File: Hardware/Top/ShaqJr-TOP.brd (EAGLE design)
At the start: 38 x 38 mm, 65 parts, among them SW3 SWITCH.MOM, SW4 SWITCH.MOM, U1 NRF52832_MODULE_MDBT42, U2 PCF8523, U3 FT231XS, Y1 32.768kHz, Y2 32.7680kHz

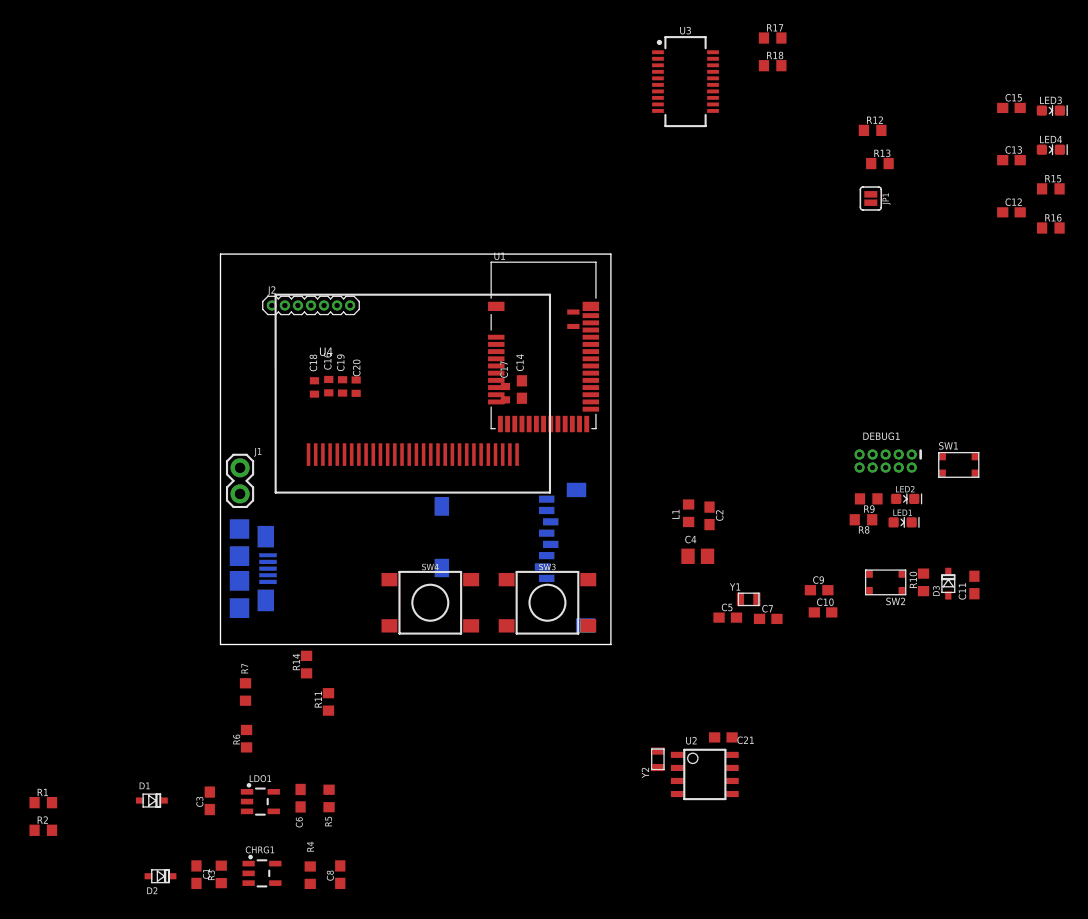
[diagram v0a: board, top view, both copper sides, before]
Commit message: completed take 007, may need to review polygons- gnd and 3.3v
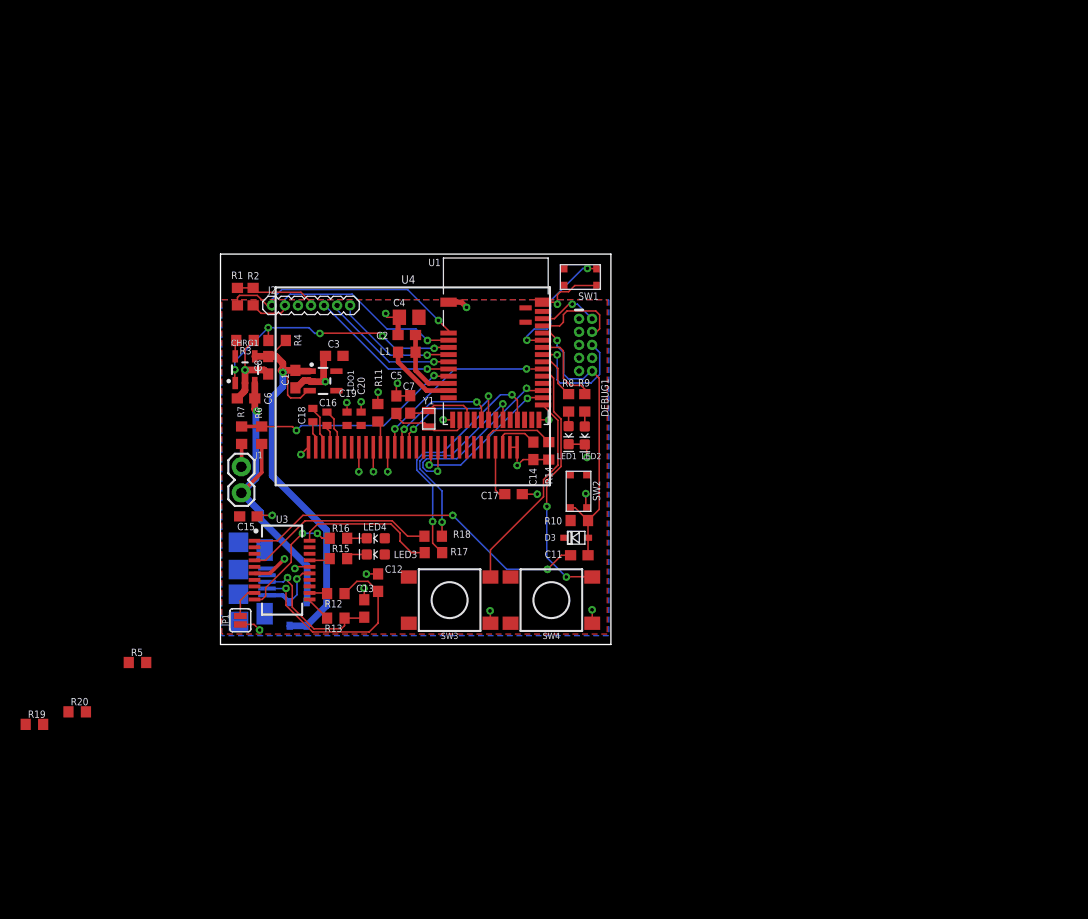
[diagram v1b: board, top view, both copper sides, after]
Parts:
- removed C10, C9: 300p, LinnesLab-Passives:C0603
- removed C21: 1u, LinnesLab-Passives:C0603
- removed SD1: (no value), LinnesLab-Connectors:MICROSD
- removed U2: PCF8523, LinnesLab-Clocks:SO8
- removed Y2: 32.7680kHz, LinnesLab-Clocks:2-SMD.NOLEAD.2.0MMTO1.2MM
- added R19, R20: 100k, LinnesLab-Passives:R0603
- C1: value 4.7u -> 1u
- C17: device LinnesLab-Passives:C0402 -> LinnesLab-Passives:C0603
- C6: value 1u -> 4.7u
- R3: value 100k -> (none)
- R4: value (none) -> 100k
- moved C15 84.2 mm to (2.72, 12.5), turned to 180 degrees
- moved LED3 78.6 mm to (15.1, 8.76), turned to 180 degrees
- moved R15 78.1 mm to (11.5, 8.36)
- moved C13 76.6 mm to (14.0, 3.51), turned to 90 degrees
- moved LED4 75.8 mm to (15.1, 10.3), turned to 180 degrees
- moved R16 75.6 mm to (11.5, 10.3)
- moved JP1 73.8 mm to (1.93, 2.36), turned to 90 degrees
- moved C12 71.4 mm to (15.3, 6.02), turned to 270 degrees
- moved R12 69.0 mm to (11.2, 4.95), turned to 180 degrees
- moved R13 69.0 mm to (11.2, 2.57), turned to 180 degrees
- moved U3 61.7 mm to (5.99, 7.24)
- moved R17 60.0 mm to (20.7, 8.94)
- moved R18 56.5 mm to (20.7, 10.5)
- moved R2 55.8 mm to (3.17, 33.9), turned to 90 degrees
- moved R1 52.8 mm to (1.65, 33.9), turned to 90 degrees
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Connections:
- removed net A6/TIA: J2.6, U1.7
- removed net A7/PPG: J2.7, U1.8
- removed net CD2: SD1.CD2
- removed net D29/LED.CTRL: J2.5, U1.6
- removed net N$2: R18.1
- removed net N$22: U2.1, Y2.P$2
- removed net N$3: R2.1
- removed net N$5: U2.2, Y2.P$1
- removed net VBAT: U2.3
- new net A4/PPG: J2.7, U1.5
- new net A5/TIA: J2.6, U1.6
- new net A7/BATT: R6.1, R7.2, U1.8
- new net D30/LED.CTRL: J2.5, U1.7
- net 3.3V: now also C3.1, R20.2; no longer C21.1, C6.1, R5.2, SD1.4, U2.8
- net A4/BATT: now also R19.2, R5.1; no longer R6.1, R7.2, U1.5
- net D27/CHRG.STATUS: now also R4.1; no longer R3.1
- net D5/CD1: no longer SD1.CD1
- net D7/SD.CS: no longer SD1.2
- net GND: now also C3.2, C8.1, R19.1, R20.1, R3.1; no longer C10.2, C21.2, C3.1, C8.2, C9.2, R4.1, R5.1, SD1.6, SD1.MT1, SD1.MT2, U2.4
- net MISO: no longer SD1.7
- net MOSI: no longer SD1.3
- net N$17: now also R3.2; no longer R4.2
- net P0.09/NFC1: no longer C9.1
- net P0.10/NFC2: no longer C10.1
- net RXD.FT: now also R18.1
- net SCK: no longer SD1.5
- net SCL: now also R2.1; no longer U2.6
- net SDA: no longer U2.5
- net VIN: now also C8.2, R4.2; no longer C3.2, R3.2
- net VLIPO: now also C6.1, R5.2; no longer C8.1
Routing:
- net GND: track 0.00 -> 67.2 mm, vias 0 -> 25
- net VIN: track 0.00 -> 44.1 mm, vias 0 -> 1
- net DTR: track 0.00 -> 34.5 mm, vias 0 -> 2
- net VLIPO: track 0.00 -> 30.3 mm, vias 0 -> 1
- net RESET: track 0.00 -> 29.5 mm, vias 0 -> 1
- net D27/CHRG.STATUS: track 0.00 -> 26.4 mm, vias 0 -> 5
- net SDA: track 0.00 -> 24.7 mm, vias 0 -> 1
- net D15/SW2: track 0.00 -> 24.7 mm, vias 0 -> 2
- net RXD.NRF: track 0.00 -> 24.6 mm, vias 0 -> 2
- net SCL: track 0.00 -> 22.5 mm, vias 0 -> 1
- net A7/BATT: track 0.00 -> 22.5 mm, vias 0 -> 2
- net USB-: track 0.00 -> 21.2 mm, vias 0 -> 1
- net TXD.NRF: track 0.00 -> 20.2 mm, vias 0 -> 2
- net D11/SW1: track 0.00 -> 20.1 mm
- net MOSI: track 0.00 -> 19.2 mm, vias 0 -> 2
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- added copper zone on layer 1, net 3.3V
- added copper zone on layer 16, net GND

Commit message: Finished Take 008
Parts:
- removed C19, C20: 2.2uF, LinnesLab-Passives:C0402
- removed R18: 0, LinnesLab-Passives:R0603
- removed R19, R20: 100k, LinnesLab-Passives:R0603
- removed U4: (no value), LinnesLab-Displays:UG-2864HSWEG01_0.96IN_NO-WRAPAROUND
- added C10: 47p, LinnesLab-Passives:C0603
- added C9: 100n, LinnesLab-Passives:C0603
- added U2: FT231XS, LinnesLab-DigitalIC:SSOP20_L
- C1: value 1u -> 4.7u
- C11: value 100n -> 47p
- C12: value 47p -> 10uF
- C13: value 47p -> 100n
- C14: value 10uF -> 2.2uF; device LinnesLab-Passives:C0603 -> LinnesLab-Passives:C0402
- C15: value 100n -> 2.2uF
- C17: device LinnesLab-Passives:C0603 -> LinnesLab-Passives:C0402
- C6: value 4.7u -> 1u
- R11: value 10k -> 27
- R13: value 27 -> 390k
- R14: value 390k -> 1k
- R16: value 1k -> 0
- R3: value (none) -> 100k
- R4: value 100k -> 5k
- R7: value 100k -> 1k
- R9: value 1k -> 10k
- U3: value FT231XS -> (none); device LinnesLab-DigitalIC:SSOP20_L -> LinnesLab-Displays:UG-2864HSWEG01_0.96IN_NO-WRAPAROUND
- moved R7 32.0 mm to (33.9, 23.5)
- moved R13 26.4 mm to (32.0, 18.8), turned to 270 degrees
- moved C15 25.9 mm to (28.5, 14.6)
- moved R5 25.2 mm to (4.01, 20.4), turned to 270 degrees
- moved R14 23.0 mm to (11.5, 8.36), turned to 0 degrees
- moved R10 22.2 mm to (15.3, 22.6), turned to 270 degrees
- moved C11 21.6 mm to (14.0, 3.51), turned to 90 degrees
- moved C14 20.3 mm to (10.4, 22.0), turned to 270 degrees
- moved C12 19.8 mm to (30.5, 18.8), turned to 90 degrees
- moved U3 18.3 mm to (18.7, 20.4), turned to 0 degrees
- moved R11 18.1 mm to (11.2, 4.95), turned to 180 degrees
- moved C17 17.8 mm to (12.3, 22.0), turned to 270 degrees
- moved C13 14.4 mm to (2.72, 12.5), turned to 180 degrees
- moved R9 11.5 mm to (34.9, 12.1), turned to 180 degrees
- moved C6 9.53 mm to (11.1, 28.1)
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- renumbered SW2 to RESET
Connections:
- removed net A4/BATT: R19.2, R5.1
- net !CTS: now also U2.9; no longer U3.9
- net 3.3V: now also C13.2, C17.2, C18.2, C6.1, R9.2, U2.14, U2.3, U3.6, U3.9; no longer C15.2, C19.2, C20.2, C3.1, R10.2, R20.2, U3.14, U3.3, U4.6, U4.9
- net A7/BATT: now also R5.1, R6.2; no longer R6.1, R7.2
- net D16/CS.OLED: now also U3.13; no longer U4.13
- net D27/CHRG.STATUS: now also R3.1; no longer R4.1
- net D3/RESET.OLED: now also U3.14; no longer U4.14
- net D4/DC.OLED: now also U3.15; no longer U4.15
- net DTR: now also C9.1, U2.1; no longer C11.1, U3.1
- net FT3V3: now also U2.13; no longer U3.13
- net GND: now also C10.1, C11.2, C13.1, C18.1, C3.1, C8.2, R10.1, R13.2, R4.1, R6.1, U2.16, U2.6, U3.1, U3.10, U3.12, U3.29, U3.30, U3.8; no longer C13.2, C14.1, C19.1, C20.1, C3.2, C8.1, R11.1, R14.2, R19.1, R20.1, R3.1, R7.1, U3.16, U3.6, U4.1, U4.10, U4.12, U4.29, U4.30, U4.8
- net LED1: now also R7.2; no longer R8.2
- net LED2: now also R8.2; no longer R9.2
- net MOSI: now also U3.19; no longer U4.19
- net N$10: now also C16.1, U3.3; no longer C18.1, U4.3
- net N$11: now also C14.2, U3.4; no longer C16.2, U4.4
- net N$12: now also C14.1, U3.5; no longer C16.1, U4.5
- net N$14: now also C12.2, U3.28; no longer C14.2, U4.28
- net N$15: now also C15.2, U3.27; no longer C17.2, U4.27
- net N$17: now also R4.2; no longer R3.2
- net N$18: now also R14.2; no longer R15.2
- net N$21: now also R15.2; no longer R16.2
- net N$29: now also R7.1; no longer R8.1
- net N$30: now also R8.1; no longer R9.1
- net N$4: now also R10.2, U3.11; no longer R11.2, U4.11
- net N$6: now also R13.1, U3.26; no longer R14.1, U4.26
- net N$7: now also R11.2, U2.12; no longer R12.2, U3.12
- net N$8: now also R12.2, U2.11; no longer R13.2, U3.11
- net N$9: now also C16.2, U3.2; no longer C18.2, U4.2
- net RESET: now also C9.2, R9.1; no longer C11.2, R10.1
- net RXD.FT: now also R17.1, U2.4; no longer R18.1, U3.4
- net RXD.NRF: now also R16.2; no longer R17.2
- net RXLED: now also R14.1, U2.17; no longer R15.1, U3.17
- net SCK: now also U3.18; no longer U4.18
- net TXD.FT: now also R16.1, U2.20; no longer R17.1, U3.20
- net TXD.NRF: now also R17.2; no longer R18.2
- net TXLED: now also R15.1, U2.10; no longer R16.1, U3.10
- net USB+: now also C11.1, R12.1; no longer C13.1, R13.1
- net USB-: now also C10.2, R11.1; no longer C12.2, R12.1
- net VIN: now also C3.2, R3.2; no longer C8.2, R4.2
- net VLIPO: now also C8.1; no longer C6.1, R6.2
- net V_USB: now also U2.15; no longer U3.15
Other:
- board text added: "+"
